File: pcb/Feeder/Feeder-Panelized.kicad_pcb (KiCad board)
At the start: 2 copper layers, 99 x 98.8 mm, 270 parts, among them J1 Controller, J10 Controller, J100 Controller, J101 N20, J102 Servo/Feedback, J103 Controller, J104 N20, J105 Servo/Feedback, J106 Controller, J107 N20, J108 Servo/Feedback, J109 Controller, J11 N20, J110 N20, J111 Servo/Feedback, J112 Controller, J113 N20, J114 Servo/Feedback, J115 Controller, J116 N20, J117 Servo/Feedback, J118 Controller, J119 N20, J12 Servo/Feedback, J120 Servo/Feedback, J13 Controller, J14 N20, J15 Servo/Feedback, J16 Controller, J17 N20, J18 Servo/Feedback, J19 Controller, J2 N20, J20 N20, J21 Servo/Feedback, J22 Controller, J23 N20, J24 Servo/Feedback, J25 Controller, J26 N20, J27 Servo/Feedback, J28 Controller, J29 N20, J3 Servo/Feedback, J30 Servo/Feedback, J31 Controller, J32 N20, J33 Servo/Feedback, J34 Controller, J35 N20, J36 Servo/Feedback, J37 Controller, J38 N20, J39 Servo/Feedback, J4 Controller, J40 Controller, J41 N20, J42 Servo/Feedback, J43 Controller, J44 N20, J45 Servo/Feedback, J46 Controller, J47 N20, J48 Servo/Feedback, J49 Controller, J5 N20, J50 N20, J51 Servo/Feedback, J52 Controller, J53 N20, J54 Servo/Feedback, J55 Controller, J56 N20, J57 Servo/Feedback, J58 Controller, J59 N20, J6 Servo/Feedback, J60 Servo/Feedback, J61 Controller, J62 N20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

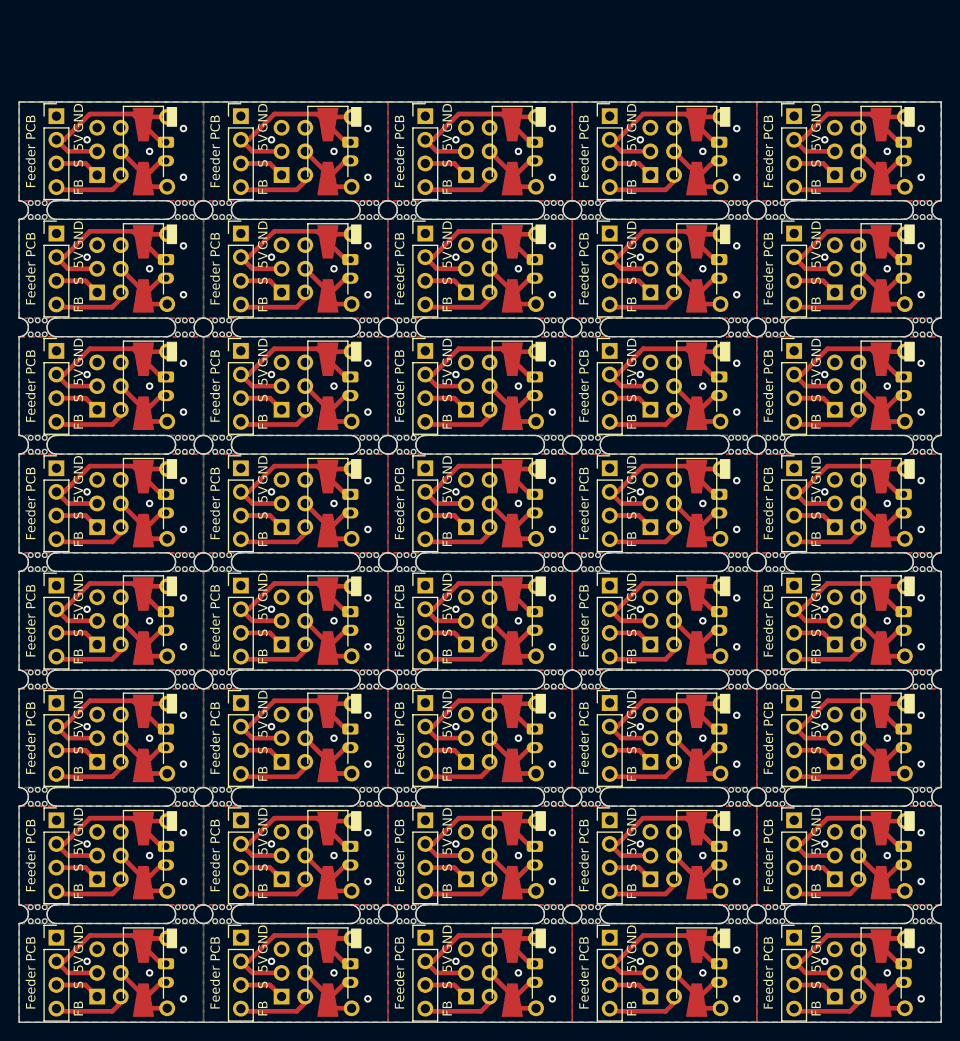
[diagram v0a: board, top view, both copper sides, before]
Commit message: recreated feeder PCB for new 0816 CAD design (#5)
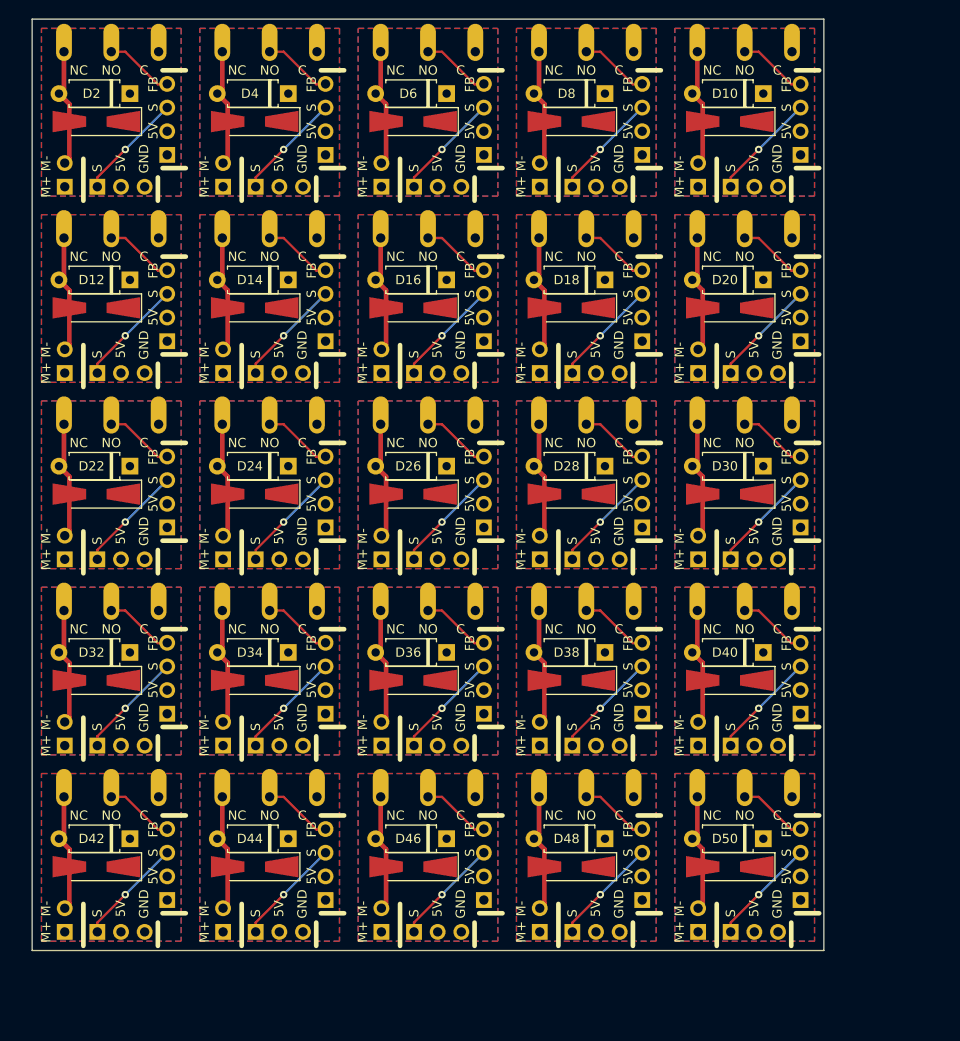
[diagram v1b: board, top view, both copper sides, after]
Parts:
- removed D51, D53, D55, D57, D59, D61, D63, D65, D67, D69, D71, D73, D75, D77, D79: 1N4001, Diode_SMD:D_SMA-SMB_Universal_Handsoldering
- removed D52, D54, D56, D58, D60, D62, D64, D66, D68, D70, D72, D74, D76, D78, D80: 1N4001, CustomDiode:D_SMA-SMB_Universal_Handsoldering_Holes
- removed J100, J103, J106, J109, J112, J115, J118, J76, J79, J82, J85, J88, J91, J94, J97: Controller, Connector_PinHeader_2.54mm:PinHeader_1x04_P2.54mm_Vertical
- removed J101, J104, J107, J110, J113, J116, J119, J77, J80, J83, J86, J89, J92, J95, J98: N20, Connector_JST:JST_PH_B2B-PH-K_1x02_P2.00mm_Vertical
- removed J102, J105, J108, J111, J114, J117, J120, J78, J81, J84, J87, J90, J93, J96, J99: Servo/Feedback, Connector_PinHeader_2.54mm:PinHeader_2x03_P2.54mm_Vertical
- removed mouse-bite-2mm-slot (x2), mouse-bite-2mm-slot1, mouse-bite-2mm-slot10, mouse-bite-2mm-slot11, mouse-bite-2mm-slot12, mouse-bite-2mm-slot13, mouse-bite-2mm-slot14, mouse-bite-2mm-slot15, mouse-bite-2mm-slot16, mouse-bite-2mm-slot17, mouse-bite-2mm-slot18, mouse-bite-2mm-slot19, mouse-bite-2mm-slot2, mouse-bite-2mm-slot20, mouse-bite-2mm-slot21, mouse-bite-2mm-slot22, mouse-bite-2mm-slot23, mouse-bite-2mm-slot24, mouse-bite-2mm-slot25, mouse-bite-2mm-slot26, mouse-bite-2mm-slot27, mouse-bite-2mm-slot28, mouse-bite-2mm-slot29, mouse-bite-2mm-slot3, mouse-bite-2mm-slot30, mouse-bite-2mm-slot31, mouse-bite-2mm-slot32, mouse-bite-2mm-slot33, mouse-bite-2mm-slot34, mouse-bite-2mm-slot35, mouse-bite-2mm-slot36, mouse-bite-2mm-slot37, mouse-bite-2mm-slot38, mouse-bite-2mm-slot39, mouse-bite-2mm-slot4, mouse-bite-2mm-slot40, mouse-bite-2mm-slot41, mouse-bite-2mm-slot42, mouse-bite-2mm-slot43, mouse-bite-2mm-slot44, mouse-bite-2mm-slot45, mouse-bite-2mm-slot46, mouse-bite-2mm-slot47, mouse-bite-2mm-slot48, mouse-bite-2mm-slot49, mouse-bite-2mm-slot5, mouse-bite-2mm-slot50, mouse-bite-2mm-slot51, mouse-bite-2mm-slot52, mouse-bite-2mm-slot53, mouse-bite-2mm-slot54, mouse-bite-2mm-slot55, mouse-bite-2mm-slot56, mouse-bite-2mm-slot57, mouse-bite-2mm-slot58, mouse-bite-2mm-slot59, mouse-bite-2mm-slot6, mouse-bite-2mm-slot60, mouse-bite-2mm-slot61, mouse-bite-2mm-slot62, mouse-bite-2mm-slot63, mouse-bite-2mm-slot64, mouse-bite-2mm-slot65, mouse-bite-2mm-slot66, mouse-bite-2mm-slot67, mouse-bite-2mm-slot68, mouse-bite-2mm-slot7, mouse-bite-2mm-slot8, mouse-bite-2mm-slot9: VAL**, Panelization:mouse-bite-2mm-slot
- added SW1: SW_SPDT, Microswitch:Microswitch, F.Cu at (153.1, 83.5)
- added SW10: SW_SPDT, Microswitch:Microswitch, F.Cu at (221.1, 103.5)
- added SW11: SW_SPDT, Microswitch:Microswitch, F.Cu at (153.1, 123.5)
- added SW12: SW_SPDT, Microswitch:Microswitch, F.Cu at (170.1, 123.5)
- added SW13: SW_SPDT, Microswitch:Microswitch, F.Cu at (187.1, 123.5)
- added SW14: SW_SPDT, Microswitch:Microswitch, F.Cu at (204.1, 123.5)
- added SW15: SW_SPDT, Microswitch:Microswitch, F.Cu at (221.1, 123.5)
- added SW16: SW_SPDT, Microswitch:Microswitch, F.Cu at (153.1, 143.5)
- added SW17: SW_SPDT, Microswitch:Microswitch, F.Cu at (170.1, 143.5)
- added SW18: SW_SPDT, Microswitch:Microswitch, F.Cu at (187.1, 143.5)
- added SW19: SW_SPDT, Microswitch:Microswitch, F.Cu at (204.1, 143.5)
- added SW2: SW_SPDT, Microswitch:Microswitch, F.Cu at (170.1, 83.5)
- added SW20: SW_SPDT, Microswitch:Microswitch, F.Cu at (221.1, 143.5)
- added SW21: SW_SPDT, Microswitch:Microswitch, F.Cu at (153.1, 163.5)
- added SW22: SW_SPDT, Microswitch:Microswitch, F.Cu at (170.1, 163.5)
- added SW23: SW_SPDT, Microswitch:Microswitch, F.Cu at (187.1, 163.5)
- added SW24: SW_SPDT, Microswitch:Microswitch, F.Cu at (204.1, 163.5)
- added SW25: SW_SPDT, Microswitch:Microswitch, F.Cu at (221.1, 163.5)
- added SW3: SW_SPDT, Microswitch:Microswitch, F.Cu at (187.1, 83.5)
- added SW4: SW_SPDT, Microswitch:Microswitch, F.Cu at (204.1, 83.5)
- added SW5: SW_SPDT, Microswitch:Microswitch, F.Cu at (221.1, 83.5)
- added SW6: SW_SPDT, Microswitch:Microswitch, F.Cu at (153.1, 103.5)
- added SW7: SW_SPDT, Microswitch:Microswitch, F.Cu at (170.1, 103.5)
- added SW8: SW_SPDT, Microswitch:Microswitch, F.Cu at (187.1, 103.5)
- added SW9: SW_SPDT, Microswitch:Microswitch, F.Cu at (204.1, 103.5)
- D10, D12, D14, D16, D18, D2, D20, D22, D24, D26, D28, D30, D32, D34, D36, D38, D4, D40, D42, D44, D46, D48, D50, D6, D8: footprint CustomDiode:D_SMA-SMB_Universal_Handsoldering_Holes -> Diode_THT:D_A-405_P7.62mm_Horizontal
- J1, J10, J13, J16, J19, J22, J25, J28, J31, J34, J37, J40, J43, J46, J49, J52, J55, J58, J61, J64, J67, J7, J70, J73: value Controller -> Conn_01x03_Male; footprint Connector_PinHeader_2.54mm:PinHeader_1x04_P2.54mm_Vertical -> PinsClean:PinSocket_1x03_P2.54mm_Vertical_Clean
- J11, J14, J17, J2, J20, J23, J26, J29, J32, J35, J38, J41, J44, J47, J5, J50, J53, J56, J59, J62, J65, J68, J71, J74, J8: footprint Connector_JST:JST_PH_B2B-PH-K_1x02_P2.00mm_Vertical -> PinsClean:PinSocket_1x02_P2.54mm_Vertical_Clean; moved to F.Cu
- J12, J15, J18, J21, J24, J27, J30, J33, J36, J39, J42, J45, J48, J51, J54, J57, J6, J60, J63, J66, J69, J72, J75, J9: value Servo/Feedback -> Conn_01x04; footprint Connector_PinHeader_2.54mm:PinHeader_2x03_P2.54mm_Vertical -> PinsClean:PinSocket_1x04_P2.54mm_Vertical_Clean; moved to F.Cu
- J3: value Servo/Feedback -> Conn_01x03_Male; footprint Connector_PinHeader_2.54mm:PinHeader_2x03_P2.54mm_Vertical -> PinsClean:PinSocket_1x03_P2.54mm_Vertical_Clean; moved to F.Cu
- J4: value Controller -> Conn_01x04; footprint Connector_PinHeader_2.54mm:PinHeader_1x04_P2.54mm_Vertical -> PinsClean:PinSocket_1x04_P2.54mm_Vertical_Clean
- moved J74 40.9 mm to (211.0, 178.0), turned to 180 degrees
- moved J71 39.4 mm to (194.0, 178.0), turned to 180 degrees
- moved J68 38.1 mm to (177.0, 178.0), turned to 180 degrees
- moved J73 37.8 mm to (214.5, 178.0), turned to 90 degrees
- moved J61 37.4 mm to (146.5, 178.0), turned to 90 degrees
- moved J70 37.4 mm to (197.5, 178.0), turned to 90 degrees
- moved J64 37.2 mm to (163.5, 178.0), turned to 90 degrees
- moved J67 37.2 mm to (180.5, 178.0), turned to 90 degrees
- moved J65 37.0 mm to (160.0, 178.0), turned to 180 degrees
- moved J62 36.1 mm to (143.0, 178.0), turned to 180 degrees
- moved J59 34.9 mm to (211.0, 158.0), turned to 180 degrees
- moved J56 33.2 mm to (194.0, 158.0), turned to 180 degrees
- moved J53 31.6 mm to (177.0, 158.0), turned to 180 degrees
- moved D49 31.0 mm to (214.4, 171.0), turned to 180 degrees
- moved J58 30.5 mm to (214.5, 158.0), turned to 90 degrees
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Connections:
- J1 pad 1: GND -> /SERVO
- J1 pad 3: /SERVO -> GND
- J10 pad 1: GND -> /SERVO
- J10 pad 3: /SERVO -> GND
- J12 pad 1: /SERVO -> GND
- J12 pad 2: /FEEDBACK -> +5V
- J12 pad 3: +5V -> /SERVO
- J12 pad 4: /N20-GND -> /FEEDBACK
- J13 pad 1: GND -> /SERVO
- J13 pad 3: /SERVO -> GND
- J15 pad 1: /SERVO -> GND
- J15 pad 2: /FEEDBACK -> +5V
- J15 pad 3: +5V -> /SERVO
- J15 pad 4: /N20-GND -> /FEEDBACK
- J16 pad 1: GND -> /SERVO
- J16 pad 3: /SERVO -> GND
- J18 pad 1: /SERVO -> GND
- J18 pad 2: /FEEDBACK -> +5V
- J18 pad 3: +5V -> /SERVO
- J18 pad 4: /N20-GND -> /FEEDBACK
- J19 pad 1: GND -> /SERVO
- J19 pad 3: /SERVO -> GND
- J21 pad 1: /SERVO -> GND
- J21 pad 2: /FEEDBACK -> +5V
- J21 pad 3: +5V -> /SERVO
- J21 pad 4: /N20-GND -> /FEEDBACK
- J22 pad 1: GND -> /SERVO
- J22 pad 3: /SERVO -> GND
- J24 pad 1: /SERVO -> GND
- J24 pad 2: /FEEDBACK -> +5V
- J24 pad 3: +5V -> /SERVO
- J24 pad 4: /N20-GND -> /FEEDBACK
- J25 pad 1: GND -> /SERVO
- J25 pad 3: /SERVO -> GND
- J27 pad 1: /SERVO -> GND
- J27 pad 2: /FEEDBACK -> +5V
- J27 pad 3: +5V -> /SERVO
- J27 pad 4: /N20-GND -> /FEEDBACK
- J28 pad 1: GND -> /SERVO
- J28 pad 3: /SERVO -> GND
- J3 pad 2: /FEEDBACK -> +5V
- J3 pad 3: +5V -> GND
- J30 pad 1: /SERVO -> GND
- J30 pad 2: /FEEDBACK -> +5V
- J30 pad 3: +5V -> /SERVO
- J30 pad 4: /N20-GND -> /FEEDBACK
- J31 pad 1: GND -> /SERVO
- J31 pad 3: /SERVO -> GND
- J33 pad 1: /SERVO -> GND
- J33 pad 2: /FEEDBACK -> +5V
- J33 pad 3: +5V -> /SERVO
- J33 pad 4: /N20-GND -> /FEEDBACK
- J34 pad 1: GND -> /SERVO
- J34 pad 3: /SERVO -> GND
- J36 pad 1: /SERVO -> GND
- J36 pad 2: /FEEDBACK -> +5V
- J36 pad 3: +5V -> /SERVO
- J36 pad 4: /N20-GND -> /FEEDBACK
- J37 pad 1: GND -> /SERVO
- J37 pad 3: /SERVO -> GND
- J39 pad 1: /SERVO -> GND
- J39 pad 2: /FEEDBACK -> +5V
- J39 pad 3: +5V -> /SERVO
- J39 pad 4: /N20-GND -> /FEEDBACK
- J40 pad 1: GND -> /SERVO
- J40 pad 3: /SERVO -> GND
- J42 pad 1: /SERVO -> GND
- J42 pad 2: /FEEDBACK -> +5V
- J42 pad 3: +5V -> /SERVO
- J42 pad 4: /N20-GND -> /FEEDBACK
- J43 pad 1: GND -> /SERVO
- J43 pad 3: /SERVO -> GND
- J45 pad 1: /SERVO -> GND
- J45 pad 2: /FEEDBACK -> +5V
- J45 pad 3: +5V -> /SERVO
- J45 pad 4: /N20-GND -> /FEEDBACK
- J46 pad 1: GND -> /SERVO
- J46 pad 3: /SERVO -> GND
- J48 pad 1: /SERVO -> GND
- J48 pad 2: /FEEDBACK -> +5V
- J48 pad 3: +5V -> /SERVO
- J48 pad 4: /N20-GND -> /FEEDBACK
- J49 pad 1: GND -> /SERVO
- J49 pad 3: /SERVO -> GND
- J51 pad 1: /SERVO -> GND
- J51 pad 2: /FEEDBACK -> +5V
- J51 pad 3: +5V -> /SERVO
- J51 pad 4: /N20-GND -> /FEEDBACK
- J52 pad 1: GND -> /SERVO
- J52 pad 3: /SERVO -> GND
- J54 pad 1: /SERVO -> GND
- J54 pad 2: /FEEDBACK -> +5V
- J54 pad 3: +5V -> /SERVO
- J54 pad 4: /N20-GND -> /FEEDBACK
- J55 pad 1: GND -> /SERVO
- J55 pad 3: /SERVO -> GND
- J57 pad 1: /SERVO -> GND
- J57 pad 2: /FEEDBACK -> +5V
- J57 pad 3: +5V -> /SERVO
- J57 pad 4: /N20-GND -> /FEEDBACK
- J58 pad 1: GND -> /SERVO
- J58 pad 3: /SERVO -> GND
- J6 pad 1: /SERVO -> GND
- J6 pad 2: /FEEDBACK -> +5V
- J6 pad 3: +5V -> /SERVO
- J6 pad 4: /N20-GND -> /FEEDBACK
- J60 pad 1: /SERVO -> GND
- J60 pad 2: /FEEDBACK -> +5V
- J60 pad 3: +5V -> /SERVO
- J60 pad 4: /N20-GND -> /FEEDBACK
- J61 pad 1: GND -> /SERVO
- J61 pad 3: /SERVO -> GND
- J63 pad 1: /SERVO -> GND
- J63 pad 2: /FEEDBACK -> +5V
- J63 pad 3: +5V -> /SERVO
- J63 pad 4: /N20-GND -> /FEEDBACK
- J64 pad 1: GND -> /SERVO
- J64 pad 3: /SERVO -> GND
- J66 pad 1: /SERVO -> GND
- J66 pad 2: /FEEDBACK -> +5V
- J66 pad 3: +5V -> /SERVO
- J66 pad 4: /N20-GND -> /FEEDBACK
- J67 pad 1: GND -> /SERVO
- J67 pad 3: /SERVO -> GND
- J69 pad 1: /SERVO -> GND
- J69 pad 2: /FEEDBACK -> +5V
- J69 pad 3: +5V -> /SERVO
- J69 pad 4: /N20-GND -> /FEEDBACK
- J7 pad 1: GND -> /SERVO
- J7 pad 3: /SERVO -> GND
- J70 pad 1: GND -> /SERVO
- J70 pad 3: /SERVO -> GND
- J72 pad 1: /SERVO -> GND
- J72 pad 2: /FEEDBACK -> +5V
- J72 pad 3: +5V -> /SERVO
- J72 pad 4: /N20-GND -> /FEEDBACK
- J73 pad 1: GND -> /SERVO
- J73 pad 3: /SERVO -> GND
- J75 pad 1: /SERVO -> GND
- J75 pad 2: /FEEDBACK -> +5V
- J75 pad 3: +5V -> /SERVO
- J75 pad 4: /N20-GND -> /FEEDBACK
- J9 pad 1: /SERVO -> GND
- J9 pad 2: /FEEDBACK -> +5V
- J9 pad 3: +5V -> /SERVO
- J9 pad 4: /N20-GND -> /FEEDBACK
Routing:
- net +5V: track 877.5 -> 0.00 mm
- net /FEEDBACK: track 323.0 -> 186.7 mm
- net /SERVO: track 195.4 -> 290.2 mm, vias 0 -> 25
- net /N20-GND: track 401.7 -> 321.4 mm
- net GND: vias 160 -> 0
- added copper zone on F.Cu, net +5V
- removed copper zone on F.Cu, net GND
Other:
- board size 99 x 98.8 mm -> 85 x 100 mm
- board text added: "Feeder"
- board text added: "M+"
- board text added: "M-"
- board text added: "PCB"
- board text removed: "+"
- board text removed: "COM"
- board text removed: "Feeder PCB"
- board text removed: "NC"
- board text removed: "NO"
